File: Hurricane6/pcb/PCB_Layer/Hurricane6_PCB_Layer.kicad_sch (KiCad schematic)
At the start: 18 parts, among them SW1 SW_1, SW2 SW_2, SW3 SW_3, SW4 SW_4, SW5 SW_5, SW6 SW_6, U1 ProMicro

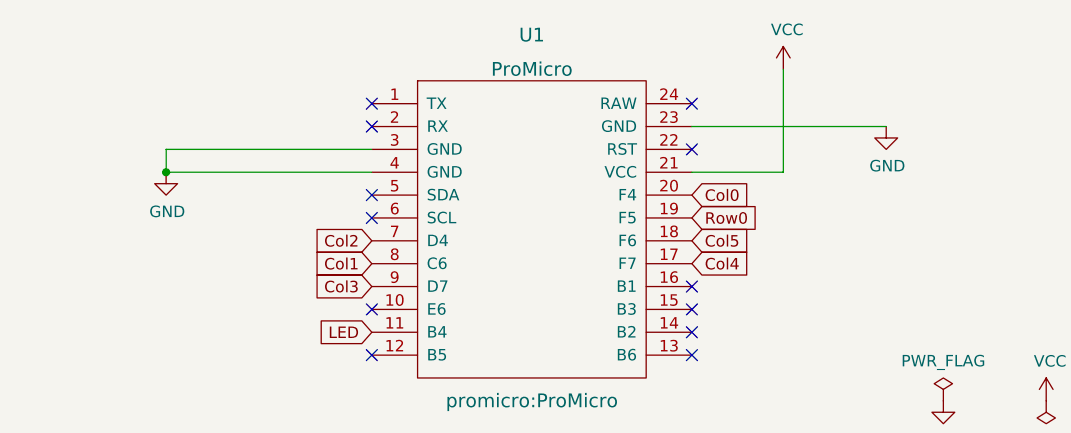
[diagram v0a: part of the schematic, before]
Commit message: feat: wiring
- consistency of wiring
- remove redundant wiring for GND(pin 3, 23)
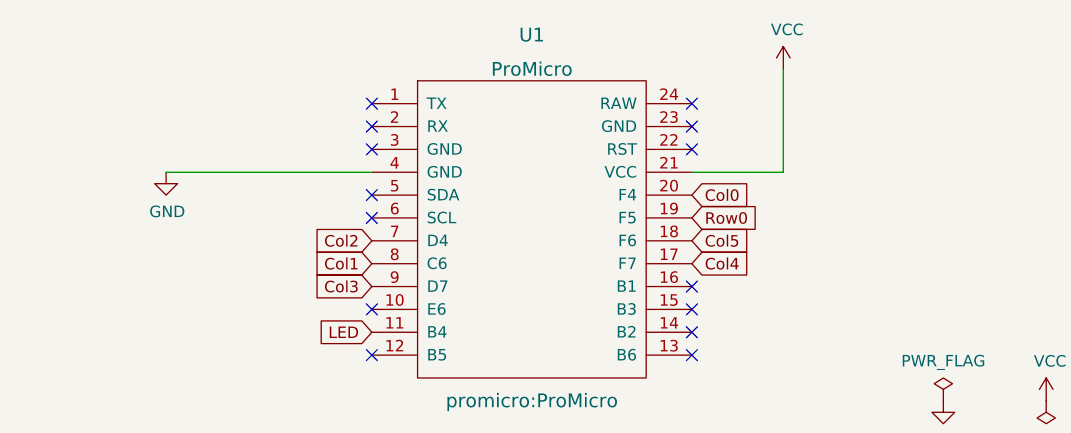
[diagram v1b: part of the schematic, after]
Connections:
- net GND: no longer U1.23 (GND), U1.3 (GND)
- no-connect marks 13 -> 15
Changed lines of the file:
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@@
   (junction (at 97.79 121.92) (diameter 0) (color 0 0 0 0)
-  )
-  (junction (at 59.69 36.83) (diameter 0) (color 0 0 0 0)
   )
   (junction (at 158.75 121.92) (diameter 0) (color 0 0 0 0)
@@
   (no_connect (at 82.55 41.91))
   (no_connect (at 118.11 52.07))
+  (no_connect (at 118.11 31.75))
   (no_connect (at 118.11 49.53))
+  (no_connect (at 82.55 34.29))
   (no_connect (at 118.11 54.61))
   (no_connect (at 82.55 31.75))
@@
   (no_connect (at 82.55 57.15))
   (no_connect (at 82.55 52.07))
-  (wire (pts (xy 82.55 34.29) (xy 59.69 34.29))
-    (stroke (width 0) (type default) (color 0 0 0 0))
-  )
   (wire (pts (xy 85.09 102.87) (xy 85.09 114.3))
     (stroke (width 0) (type default) (color 0 0 0 0))
@@
     (stroke (width 0) (type default) (color 0 0 0 0))
   )
-  (wire (pts (xy 118.11 31.75) (xy 139.7 31.75))
-    (stroke (width 0) (type default) (color 0 0 0 0))
-  )
   (wire (pts (xy 62.23 177.8) (xy 62.23 193.04))
-    (stroke (width 0) (type default) (color 0 0 0 0))
-  )
-  (wire (pts (xy 59.69 34.29) (xy 59.69 36.83))
     (stroke (width 0) (type default) (color 0 0 0 0))
   )
@@
     (pin "4")
   )
-  (symbol (lib_id "power:GND") (at 139.7 31.75 0) (unit 1)
-    (in_bom yes) (on_board yes)
-    (property "Reference" "#PWR05" (id 0) (at 139.7 38.1 0)
-      (effects (font (size 1.27 1.27)) hide)
-    )
-    (property "Value" "GND" (id 1) (at 139.827 36.1442 0))
-    (property "Footprint" "" (id 2) (at 139.7 31.75 0)
-      (effects (font (size 1.27 1.27)) hide)
-    )
-    (property "Datasheet" "" (id 3) (at 139.7 31.75 0)
-      (effects (font (size 1.27 1.27)) hide)
-    )
-    (pin "1")
-  )
   (sheet_instances
     (path "/" (page "1"))
@@
       (reference "#PWR04") (unit 1) (value "VCC") (footprint "")
     )
-    (path "/ffff14b5-2afc-4753-adbe-b74455122982"
-      (reference "#PWR05") (unit 1) (value "GND") (footprint "")
-    )
     (path "/48782386-c7f3-4695-a2d4-fdbf78cac0c5"

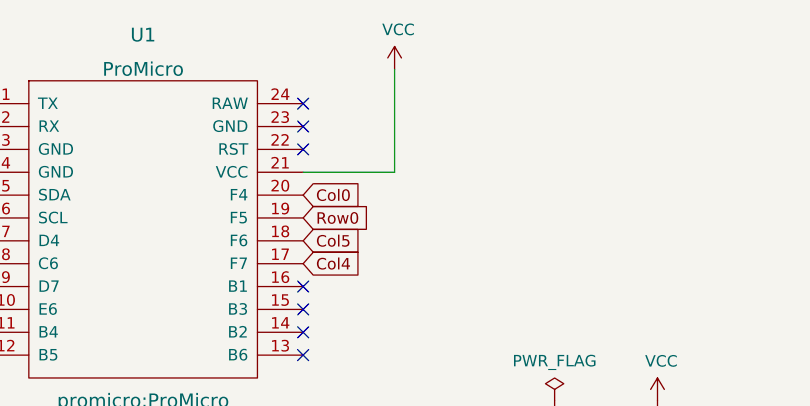
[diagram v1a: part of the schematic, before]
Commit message: featr: add reset switch and modify wiring
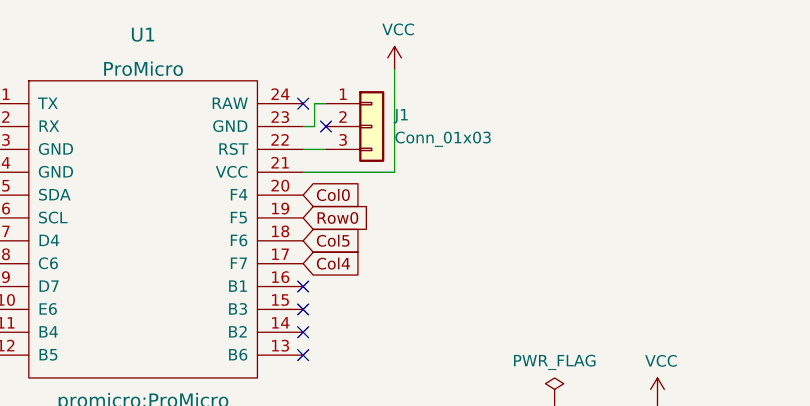
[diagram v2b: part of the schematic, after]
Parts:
- added J1: Conn_01x03, Connector_PinHeader_2.54mm:PinHeader_1x03_P2.54mm_Vertical, symbol Connector_Generic:Conn_01x03
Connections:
- net at U1.22 (RST): now also J1.3 (Pin_3)
- net at U1.23 (GND): now also J1.1 (Pin_1)
- no-connect marks 15 -> 14
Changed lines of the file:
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@@
   (no_connect (at 118.11 57.15))
   (no_connect (at 82.55 39.37))
-  (no_connect (at 118.11 29.21))
+  (no_connect (at 120.65 31.75))
   (no_connect (at 82.55 29.21))
   (no_connect (at 72.39 200.66))
   (no_connect (at 82.55 41.91))
+  (no_connect (at 118.11 29.21))
   (no_connect (at 118.11 52.07))
-  (no_connect (at 118.11 31.75))
   (no_connect (at 118.11 49.53))
   (no_connect (at 82.55 34.29))
   (no_connect (at 118.11 54.61))
   (no_connect (at 82.55 31.75))
-  (no_connect (at 118.11 34.29))
   (no_connect (at 82.55 57.15))
   (no_connect (at 82.55 52.07))
@@
     (stroke (width 0) (type default) (color 0 0 0 0))
   )
+  (wire (pts (xy 119.38 31.75) (xy 118.11 31.75))
+    (stroke (width 0) (type default) (color 0 0 0 0))
+  )
   (wire (pts (xy 105.41 114.3) (xy 107.95 114.3))
     (stroke (width 0) (type default) (color 0 0 0 0))
@@
     (stroke (width 0) (type default) (color 0 0 0 0))
   )
+  (wire (pts (xy 120.65 29.21) (xy 119.38 29.21))
+    (stroke (width 0) (type default) (color 0 0 0 0))
+  )
+  (wire (pts (xy 119.38 29.21) (xy 119.38 31.75))
+    (stroke (width 0) (type default) (color 0 0 0 0))
+  )
   (wire (pts (xy 62.23 193.04) (xy 62.23 200.66))
     (stroke (width 0) (type default) (color 0 0 0 0))
@@
   )
   (wire (pts (xy 59.69 121.92) (xy 77.47 121.92))
+    (stroke (width 0) (type default) (color 0 0 0 0))
+  )
+  (wire (pts (xy 120.65 34.29) (xy 118.11 34.29))
     (stroke (width 0) (type default) (color 0 0 0 0))
   )
@@
     (pin "4")
   )
+  (symbol (lib_id "Connector_Generic:Conn_01x03") (at 125.73 31.75 0) (unit 1)
+    (in_bom yes) (on_board yes) (fields_autoplaced)
+    (property "Reference" "J1" (id 0) (at 128.27 30.4799 0)
+      (effects (font (size 1.27 1.27)) (justify left))
+    )
+    (property "Value" "Conn_01x03" (id 1) (at 128.27 33.0199 0)
+      (effects (font (size 1.27 1.27)) (justify left))
+    )
+    (property "Footprint" "Connector_PinHeader_2.54mm:PinHeader_1x03_P2.54mm_Vertical" (id 2) (at 125.73 31.75 0)
+      (effects (font (size 1.27 1.27)) hide)
+    )
+    (property "Datasheet" "~" (id 3) (at 125.73 31.75 0)
+      (effects (font (size 1.27 1.27)) hide)
+    )
+    (pin "1")
+    (pin "2")
+    (pin "3")
+  )
   (symbol (lib_id "power:VCC") (at 157.48 62.23 0) (unit 1)
     (in_bom yes) (on_board yes)
-    (property "Reference" "#PWR07" (id 0) (at 157.48 66.04 0)
+    (property "Reference" "#PWR06" (id 0) (at 157.48 66.04 0)
       (effects (font (size 1.27 1.27)) hide)
     )
@@
   (symbol (lib_id "power:GND") (at 146.05 62.23 0) (unit 1)
     (in_bom yes) (on_board yes)
-    (property "Reference" "#PWR06" (id 0) (at 146.05 68.58 0)
+    (property "Reference" "#PWR05" (id 0) (at 146.05 68.58 0)
       (effects (font (size 1.27 1.27)) hide)
     )
@@
     )
     (path "/48782386-c7f3-4695-a2d4-fdbf78cac0c5"
-      (reference "#PWR06") (unit 1) (value "GND") (footprint "")
+      (reference "#PWR05") (unit 1) (value "GND") (footprint "")
     )
     (path "/1203f808-aed5-4540-8c9f-c2684454b89b"
-      (reference "#PWR07") (unit 1) (value "VCC") (footprint "")
+      (reference "#PWR06") (unit 1) (value "VCC") (footprint "")
     )
     (path "/17fe6c74-7093-4ce3-b0e5-cd6b76f5155b"
@@
       (reference "H7") (unit 1) (value "MountingHole") (footprint "kbd_Hole:m2_Screw_Hole")
     )
+    (path "/09caf31d-cc43-432b-8d70-26d907312904"
+      (reference "J1") (unit 1) (value "Conn_01x03") (footprint "Connector_PinHeader_2.54mm:PinHeader_1x03_P2.54mm_Vertical")
+    )
     (path "/624a8854-374a-4944-b4a8-193bf0e1a89e"
